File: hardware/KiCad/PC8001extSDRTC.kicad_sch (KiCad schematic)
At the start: 12 parts, among them J1 PC-8001 ext BUS, J2 PICkit3, J3 SD-MOD, J4 RTC-MOD, SW1 RESET_SW, U1 PIC18F47Q43

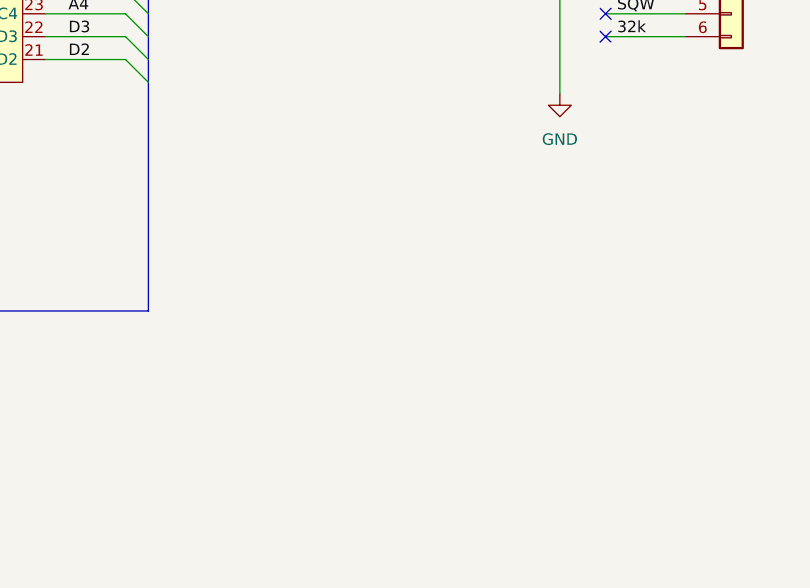
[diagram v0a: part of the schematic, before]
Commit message: feat: PCBレイアウト完成・製造用ガーバー一式を追加 #7
回路図(#6)をもとに2層基板(100x75mm)を配線。両面GNDベタ、電源0.6mm/信号0.2mm、
パスコンを各VDDピン至近(4mm前後)に配置。DRC 0違反・未配線0。
製造データ(Gerber X2/mm/4.6 + Excellonドリル + zip)を hardware/KiCad/PCB/ に同梱。
ガーバーは現行.kicad_pcbと幾何一致を確認済み。
.gitignoreにFreerouting中間(dsn/ses/rules)と空ライブラリを追加。
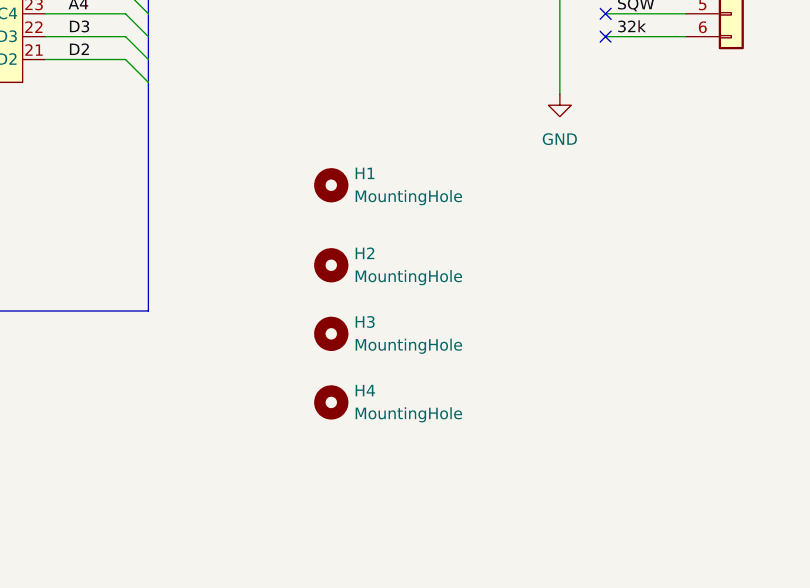
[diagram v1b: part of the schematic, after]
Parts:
- added H1, H2, H3, H4: MountingHole, MountingHole:MountingHole_3.2mm_M3, symbol Mechanical:MountingHole
- C1: footprint (none) -> Capacitor_THT:CP_Radial_D6.3mm_P2.50mm
- C2, C3, C4: footprint (none) -> Capacitor_THT:C_Disc_D3.0mm_W1.6mm_P2.50mm
- J1: footprint (none) -> Connector_PinHeader_2.54mm:PinHeader_2x25_P2.54mm_Horizontal
- J2, J3, J4: footprint (none) -> Connector_PinHeader_2.54mm:PinHeader_1x06_P2.54mm_Horizontal
- R1: footprint (none) -> Resistor_THT:R_Axial_DIN0207_L6.3mm_D2.5mm_P10.16mm_Horizontal
- SW1: footprint (none) -> Button_Switch_THT:SW_PUSH_6mm_H4.3mm
- U1: footprint (none) -> Package_DIP:DIP-40_W15.24mm_Socket
